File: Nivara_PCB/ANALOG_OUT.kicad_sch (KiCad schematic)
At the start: 21 parts, among them Q5 IRLML6402TRPBF-JSM, U12 GP8201S-TC50-EW, U13 GP8303-TC50-EW

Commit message: New changes to the Nivara PCB schematic files.
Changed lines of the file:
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@@
 	)
 	(hierarchical_label "I_OUT"
-		(shape input)
+		(shape output)
 		(at 273.05 77.47 0)
 		(effects

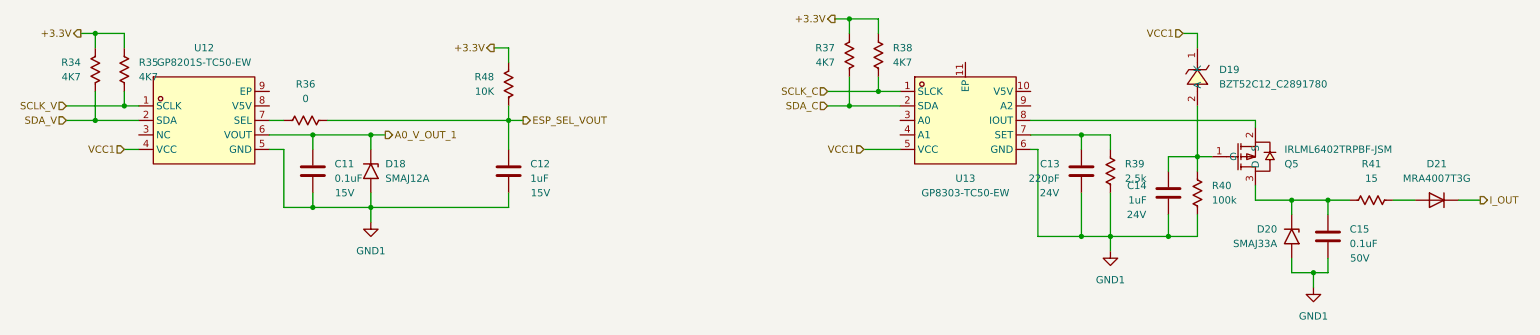
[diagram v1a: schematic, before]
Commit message: Cambios en el PCB de Nivara. Ruteo de emtradas y salidas NPN y PNP.
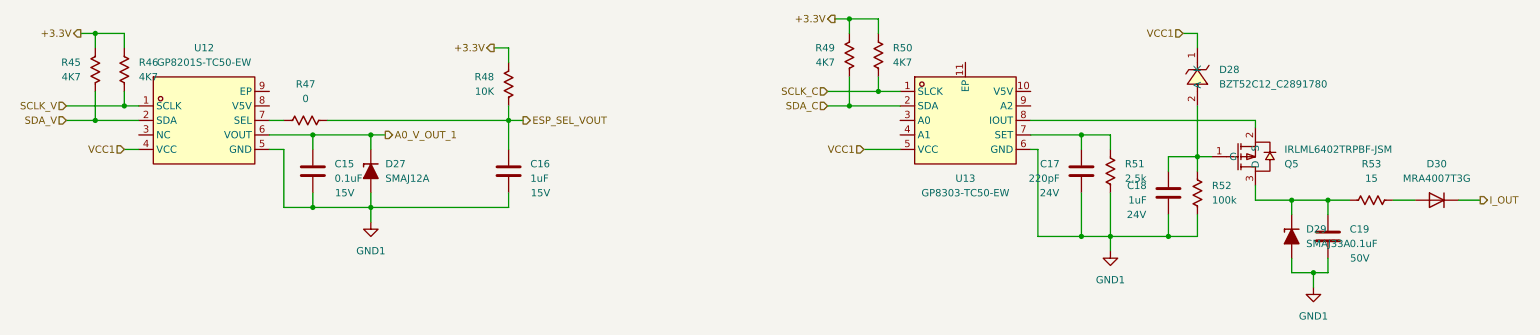
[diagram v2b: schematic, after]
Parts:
- removed D18: SMAJ12A, Diode_SMD:D_SMA, symbol Diode:SMAJ12A
- removed D20: SMAJ33A, Diode_SMD:D_SMA, symbol Diode:SMAJ33A
- added D27: SMAJ12A, PCM_Diode_SMD_AKL:D_SMA, symbol PCM_Diode_TVS_AKL:SMAJ12A
- added D29: SMAJ33A, PCM_Diode_SMD_AKL:D_SMA, symbol PCM_Diode_TVS_AKL:SMAJ33A
- renumbered C11 to C15, C12 to C16, C13 to C17, C14 to C18, C15 to C19, D19 to D28, D21 to D30, R34 to R45, R35 to R46, R36 to R47, R37 to R49, R38 to R50, R39 to R51, R40 to R52, R41 to R53
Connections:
- net A0_V_OUT_1: now also D27.1 (K)
- net GND1: now also D27.2 (A), D29.2 (A)
- net at C19.1, Q5.3 (D), R53.1: now also D29.1 (K)
